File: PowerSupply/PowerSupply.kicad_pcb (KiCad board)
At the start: 2 copper layers, 39 x 30 mm, 15 parts, among them J1 POWER, J2 VSET, J3 LASER, U0 AL8861Y-13

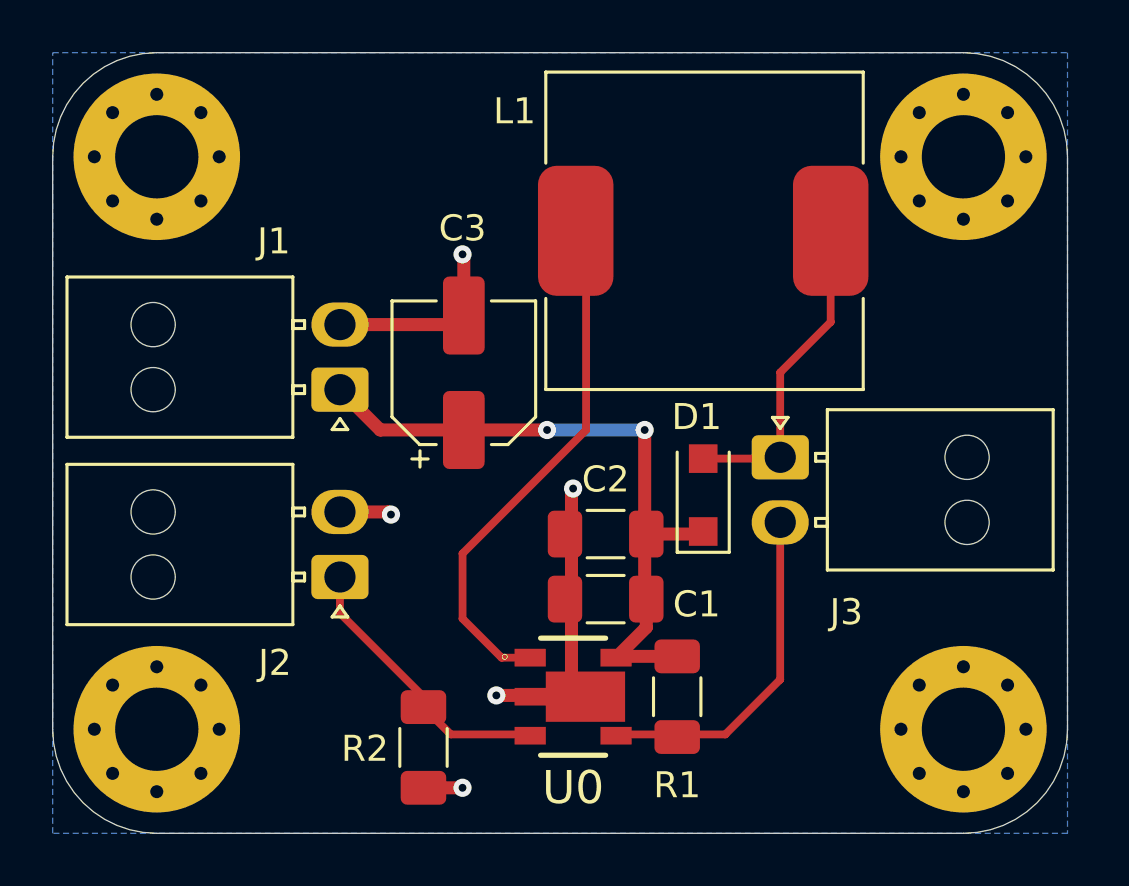
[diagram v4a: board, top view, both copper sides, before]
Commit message: Resolve comments in second review
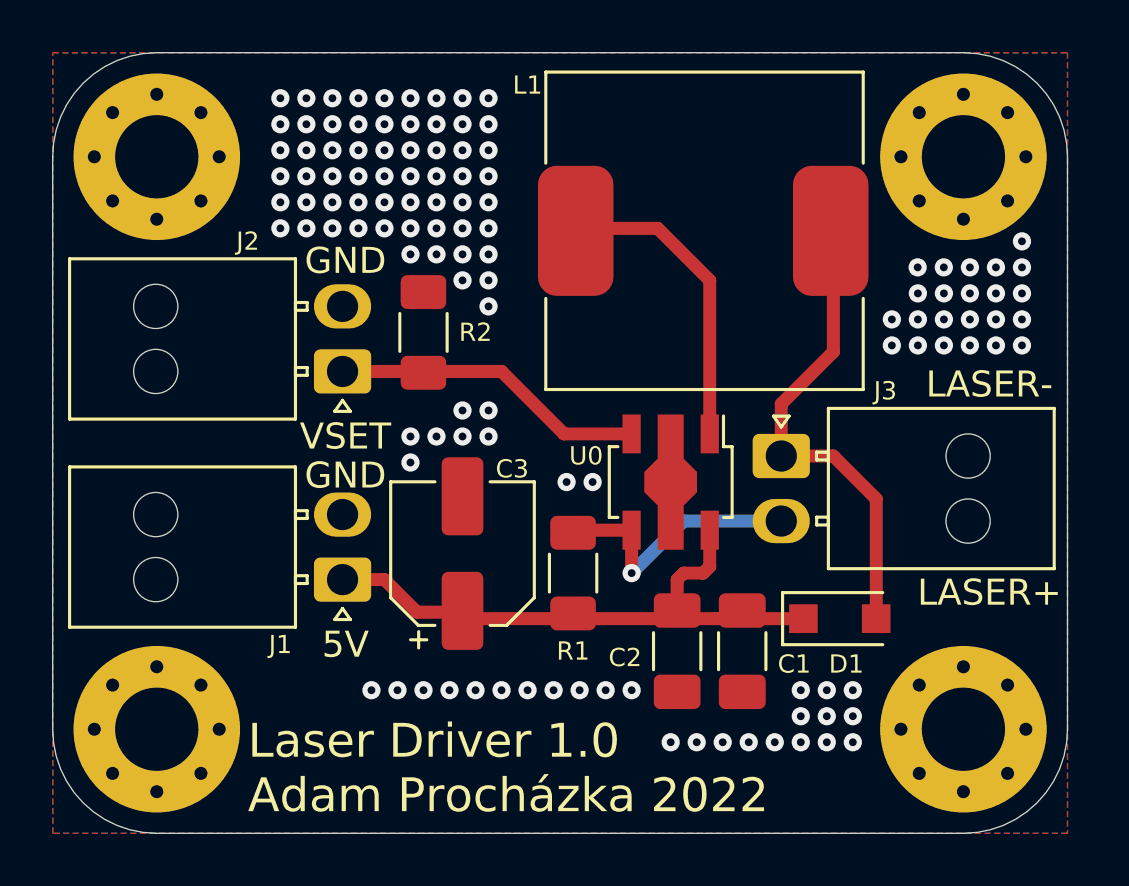
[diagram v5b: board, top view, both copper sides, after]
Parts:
- U0: footprint SamacSys_Parts:SOT89-5 -> Package_TO_SOT_SMD:SOT-89-5
- moved R2 16.0 mm to (139.2, 80.8), turned to 90 degrees
- moved U0 9.06 mm to (148.8, 86.5)
- moved J2 7.90 mm to (136.1, 82.2)
- moved J1 7.30 mm to (136.1, 90.2)
- moved D1 7.08 mm to (155.2, 91.8), turned to 0 degrees
- moved C3 6.95 mm to (140.8, 89.2)
- moved R1 6.21 mm to (145.0, 90.0), turned to 90 degrees
- moved C1 5.62 mm to (151.5, 93.0), turned to -90 degrees
- moved C2 5.27 mm to (149.0, 93.0), turned to -90 degrees
- moved J3 0.06 mm to (153.0, 85.5)
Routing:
- net GND: track 20.2 -> 0.00 mm, vias 5 -> 118
- net Net-(L1-Pad1): track 20.3 -> 11.8 mm
- net Net-(D1-Pad2): track 12.2 -> 18.5 mm
- net +5V: track 26.0 -> 22.4 mm, vias 2 -> 0
- net /ISENSE: track 13.2 -> 10.5 mm, vias 0 -> 1
- net /VSET: track 10.9 -> 12.3 mm
- added copper zone on F.Cu, net GND
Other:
- board text added: "5V"
- board text added: "GND"
- board text added: "LASER+"
- board text added: "LASER-"
- board text added: "Laser Driver 1.0 Adam Procházka 2022"
- board text added: "VSET"
- board text removed: "Ideální je mít GND plane na obou vrstvách Stačí v nastaveí plane vybrat i druhou vrstvu"
- board text removed: "Ideální je na desku přidat i popisek (vrstva silkscreen) s datem, verzí, o co se jedná a kdo je autor"
- board text removed: "Neni nutne mit extra tenke cesty, klidně by zde vsiude mohlo být 0.5mm"
- board text removed: "Pokud je to možné použijte standardní footprint Tento konkrétní v knihovnách kicadu je: Doporučuji minimálně stahovat, radši si to nakreslete sám pak neskončíte s nekvalitními footprinty Tento zrovna není ideální, z knihovny: Package_TO_SOT_SMD:SOT-89-5"
- board text removed: "Při updatu PCB ze schematu jsou nejake chyby stejne tak ERC ukazuje varování Ještě jednou poznamenávám že než mi to pošlete na review meli by vsechny kontroly ukazovat 0 chyba 0 varování Konkrétně ERC, update PCB ze schematu, DRC"
- board text removed: "Spínací cesta by měla být co nejkratší kvůli rušení a zpětné vazbě, vy ji máte nejdelší Doporučuji shlédnout: https://www.youtube.com/watch?v=AmfLhT5SntE Je to obdobné reší spínaný regulátor, což je téměř identické. Tento konkrétné obvod neumoznuje uplne ideální zapojení nicméně slo by to o hodně zlepsit"
- board text removed: "Tento prokov je zbytečný Prokovení je způsobeno už uchycením THT součástky zde V případě GND plochy na obou stranách by neměl už vůbec cenu Má cenu ovšem prokovit dvě GND plochy mezi sebou (vis stitching) Stitching je vhodný pro návratové proudy a tepelnou distribuci Plugin: https://github.com/jsreynaud/kicad-action-scripts nebo https://github.com/weirdgyn/viastitching"
- board text removed: "Titulní blok"
- board text removed: "U konektoru by měl být popisek k čemu jsou a jaké je jejih polarita Usnadní to ozivovaní a použivani"
- board text removed: "Z plosek se snazte jit pokud mozno kolmo na jejich tvar Ma to zase vliv na ruseni a u desek s uzsimi cesty i na jejich vyrobitelnost"

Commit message: update stitching
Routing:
- net GND: vias 118 -> 62
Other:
- board text added: "Profilometry - Laser diode driver Designed by: Prochazka & Malanik 08/2022 - v0.1 - STRaDe @ VUT FIT"
- board text removed: "Laser Driver 1.0 Adam Procházka 2022"

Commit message: Connection labels
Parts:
- added kibuzzard-630C99F1: G***, kibuzzard-630C99F1, B.Cu at (126.8, 89.0)
- added kibuzzard-630C9A2E: G***, kibuzzard-630C9A2E, B.Cu at (126.8, 81.0)
- added kibuzzard-630C9A4C: G***, kibuzzard-630C9A4C, B.Cu at (162.5, 86.8)
